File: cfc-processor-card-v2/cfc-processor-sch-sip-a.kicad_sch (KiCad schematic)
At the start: 33 parts, among them J5 Conn_01x04, Q1 MMBT2907, U10 TLVH431, U4 SN74AUC1G07DCKR, U7 OSD3358-1G-ISM

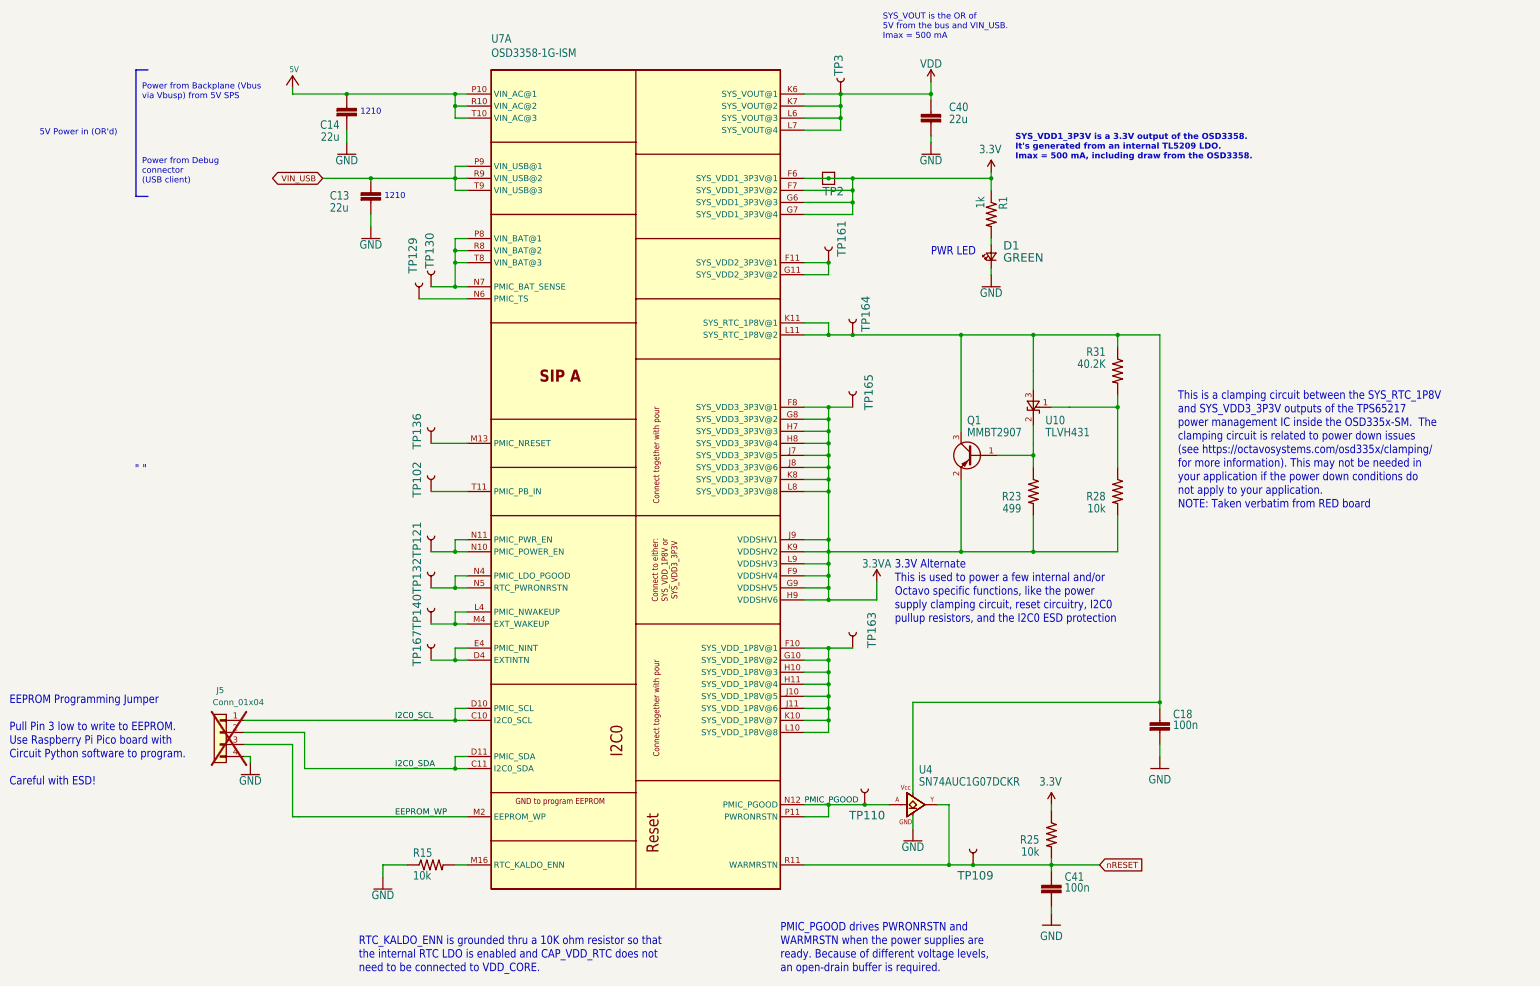
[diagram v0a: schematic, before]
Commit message: CFC processor schematic Change
changed to hierarchy view, changed all global net labels to hierarchy labels, changed all resistor, capacitor, and ground symbols to modern oresat labels. Deleted connectors sheet and added .history to gitignore.
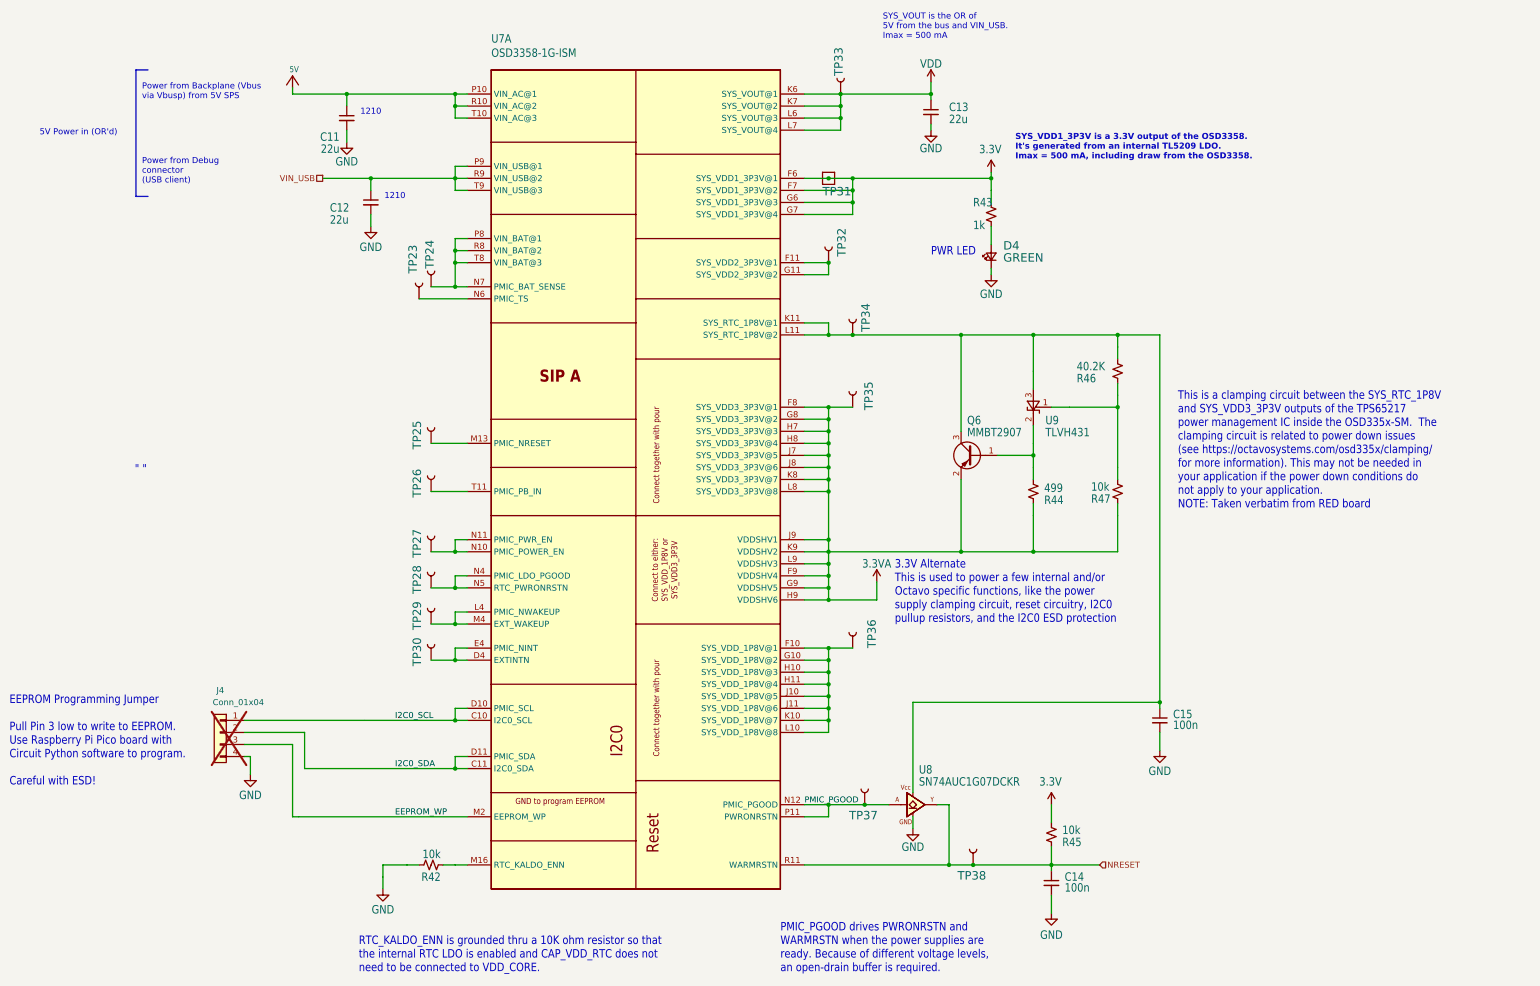
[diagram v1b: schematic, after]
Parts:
- C11: renamed from C14; symbol cfc-card-eagle-import:C-EUC1210 -> Device:C_Small
- C12: renamed from C13; symbol cfc-card-eagle-import:C-EUC1210 -> Device:C_Small
- C13: renamed from C40; symbol cfc-card-eagle-import:C-EUC1210 -> Device:C_Small
- C14: renamed from C41; symbol cfc-card-eagle-import:C-EU0603-A -> Device:C_Small
- C15: renamed from C18; symbol cfc-card-eagle-import:C-EU0603-A -> Device:C_Small
- R42: renamed from R15; symbol cfc-card-eagle-import:R-US_0603-A -> Device:R_Small_US
- R43: renamed from R1; symbol cfc-card-eagle-import:R-US_0603-A -> Device:R_Small_US
- R44: renamed from R23; symbol cfc-card-eagle-import:R-US_0603-A -> Device:R_Small_US
- R45: renamed from R25; symbol cfc-card-eagle-import:R-US_0603-A -> Device:R_Small_US
- R46: renamed from R31; symbol cfc-card-eagle-import:R-US_0603-A -> Device:R_Small_US
- R47: renamed from R28; symbol cfc-card-eagle-import:R-US_0603-A -> Device:R_Small_US
- renumbered D1 to D4, J5 to J4, Q1 to Q6, TP129 to TP23, TP130 to TP24, TP136 to TP25, TP102 to TP26, TP121 to TP27, TP132 to TP28, TP140 to TP29, TP167 to TP30, TP2 to TP31, TP161 to TP32, TP3 to TP33, TP164 to TP34, TP165 to TP35, TP163 to TP36, TP110 to TP37, TP109 to TP38, U4 to U8, U10 to U9
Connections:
- net nRESET renamed NRESET

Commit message: Updated OPD
couple of resistors and caps added to schematic. Changed USB ESD clamp VDD to 3.3v instead of octavo created VDD line.
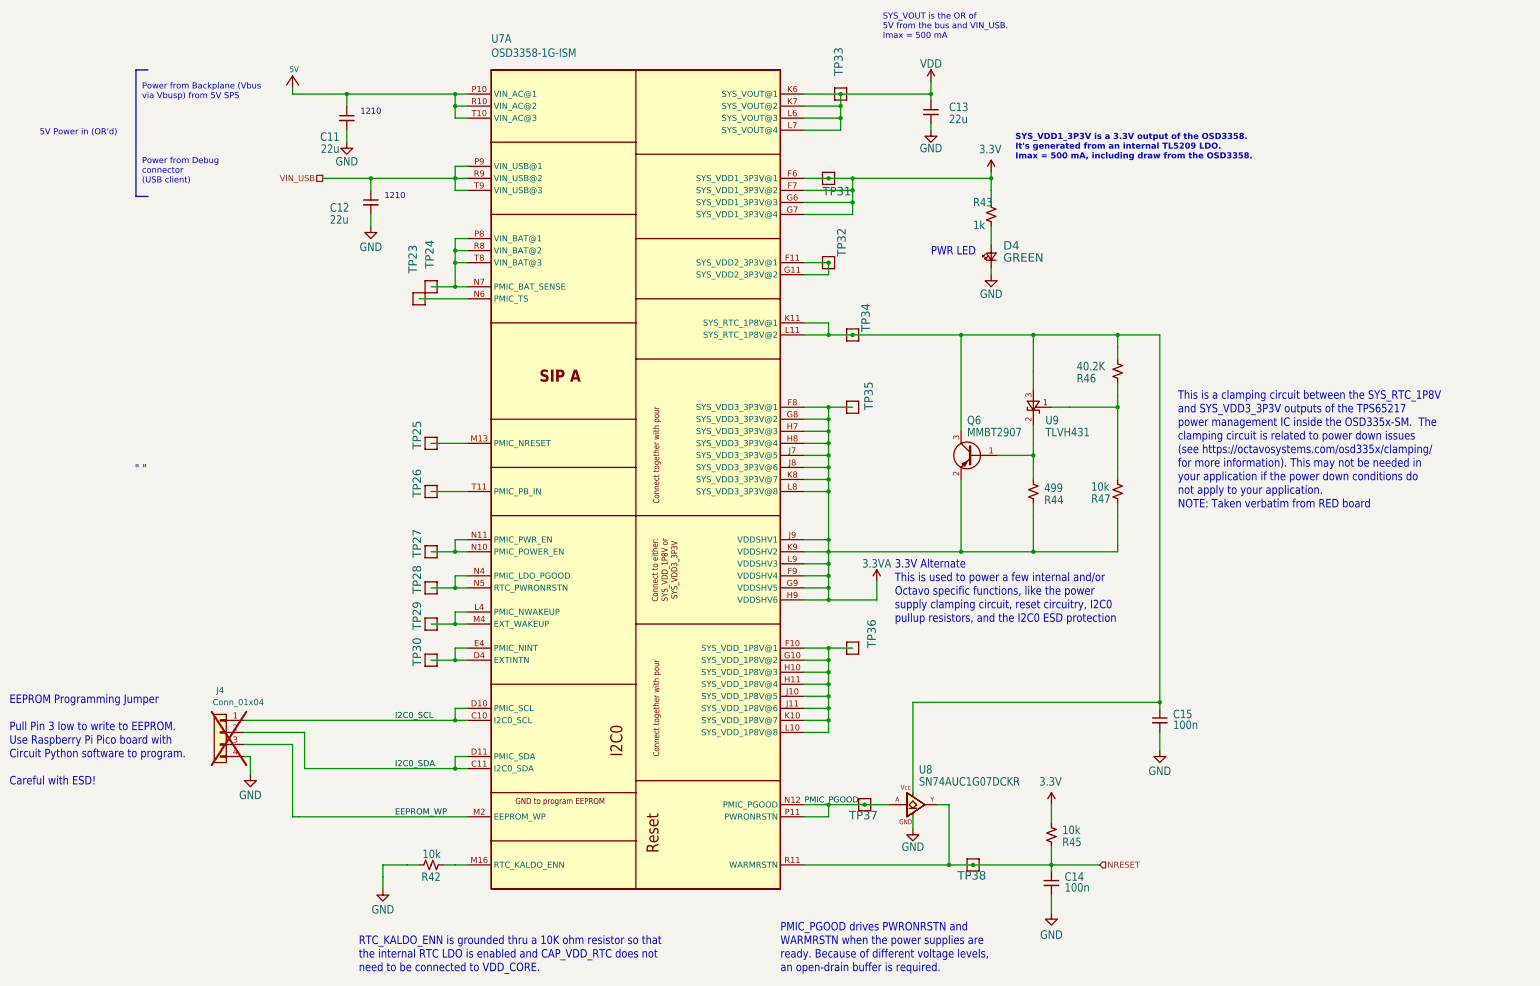
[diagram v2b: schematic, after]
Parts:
- TP23, TP24, TP25, TP26, TP27, TP28, TP29, TP30, TP32, TP33, TP34, TP35, TP36, TP37, TP38: footprint cfc-card:PAD.03X.04 -> oresat-misc:TestPoint_Pad_D1.0mm; symbol cfc-card-eagle-import:TEST-POINT3X4 -> Oresat Misc:Test-Point-1mm-round
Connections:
- net 3.3VA: now also TP35.1; no longer TP35.P$1 (1)
- net NRESET: now also TP38.1; no longer TP38.P$1 (1)
- net PMIC_PGOOD: now also TP37.1; no longer TP37.P$1 (1)
- net VDD: now also TP33.1; no longer TP33.P$1 (1)
- net at U7.D4 (EXTINTN), U7.E4 (PMIC_NINT): now also TP30.1; no longer TP30.P$1 (1)
- net at U7.F10 (SYS_VDD_1P8V@1), U7.G10 (SYS_VDD_1P8V@2), U7.H10 (SYS_VDD_1P8V@3)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: now also TP36.1; no longer TP36.P$1 (1)
- net at U7.F11 (SYS_VDD2_3P3V@1), U7.G11 (SYS_VDD2_3P3V@2): now also TP32.1; no longer TP32.P$1 (1)
- net at C15.1, Q6.3 (C), R46.1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: now also TP34.1; no longer TP34.P$1 (1)
- net at U7.L4 (PMIC_NWAKEUP), U7.M4 (EXT_WAKEUP): now also TP29.1; no longer TP29.P$1 (1)
- net at U7.M13 (PMIC_NRESET): now also TP25.1; no longer TP25.P$1 (1)
- net at U7.N10 (PMIC_POWER_EN), U7.N11 (PMIC_PWR_EN): now also TP27.1; no longer TP27.P$1 (1)
- net at U7.N4 (PMIC_LDO_PGOOD), U7.N5 (RTC_PWRONRSTN): now also TP28.1; no longer TP28.P$1 (1)
- net at U7.N6 (PMIC_TS): now also TP23.1; no longer TP23.P$1 (1)
- net at U7.N7 (PMIC_BAT_SENSE), U7.P8 (VIN_BAT@1), U7.R8 (VIN_BAT@2)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: now also TP24.1; no longer TP24.P$1 (1)
- net at U7.T11 (PMIC_PB_IN): now also TP26.1; no longer TP26.P$1 (1)

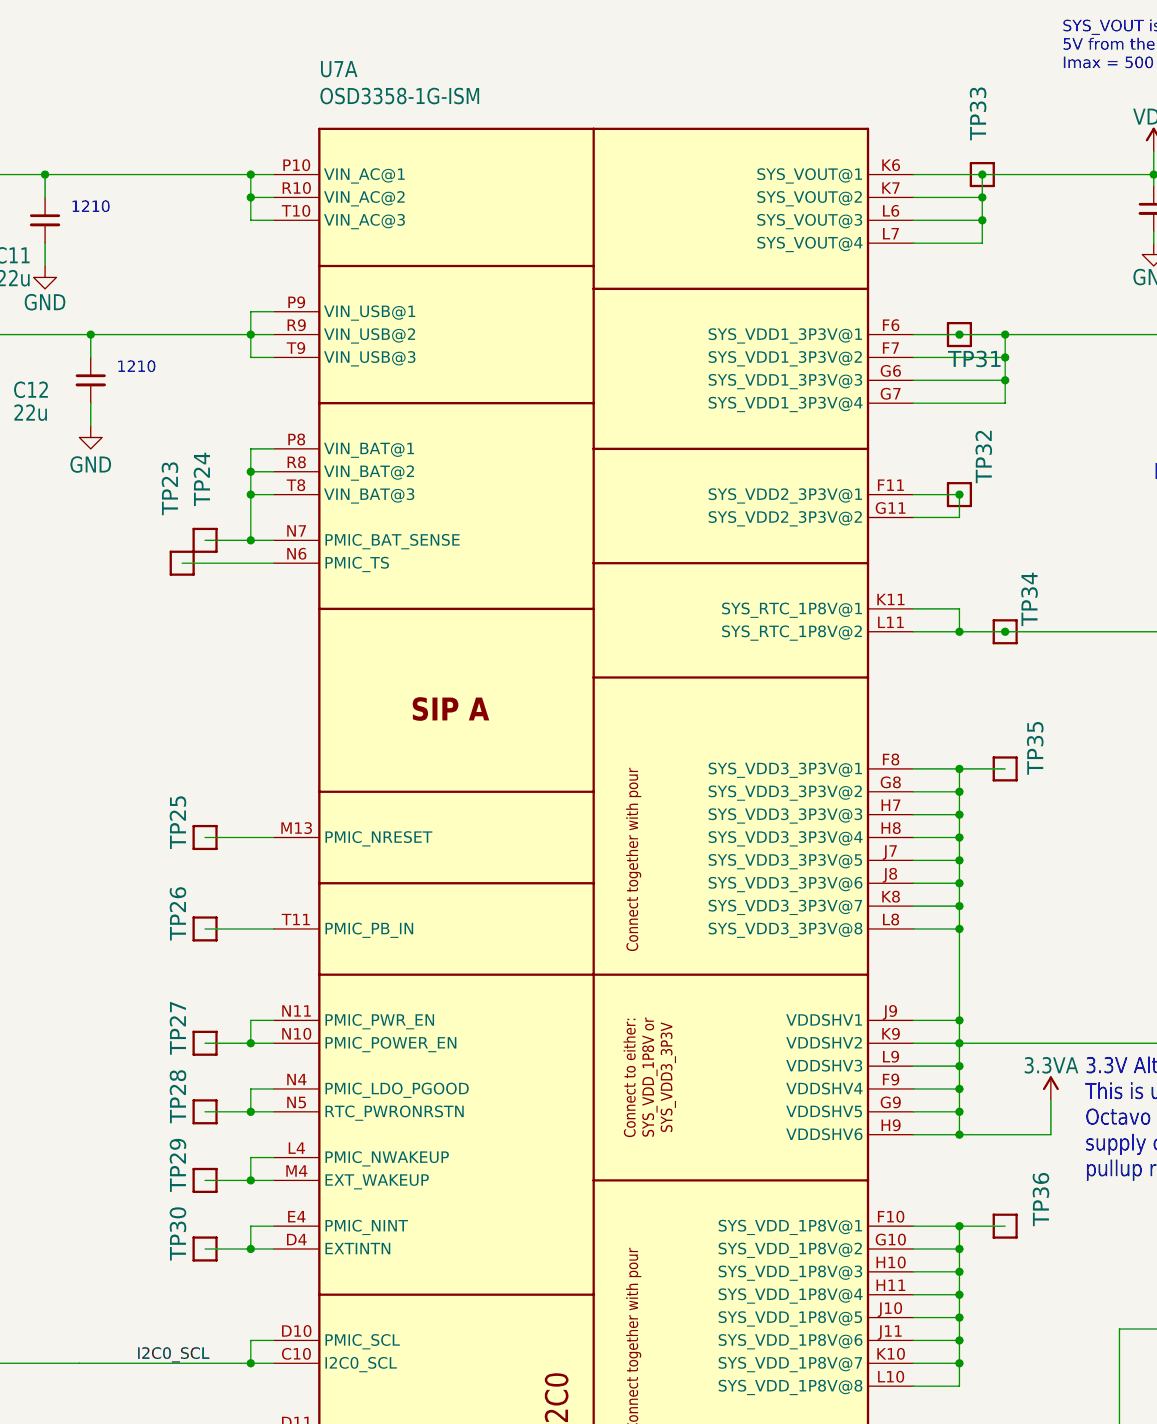
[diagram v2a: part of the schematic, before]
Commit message: Update
Added pull down resistors and removed therm + and sensor enable and added i2c support for cfc sensor card.
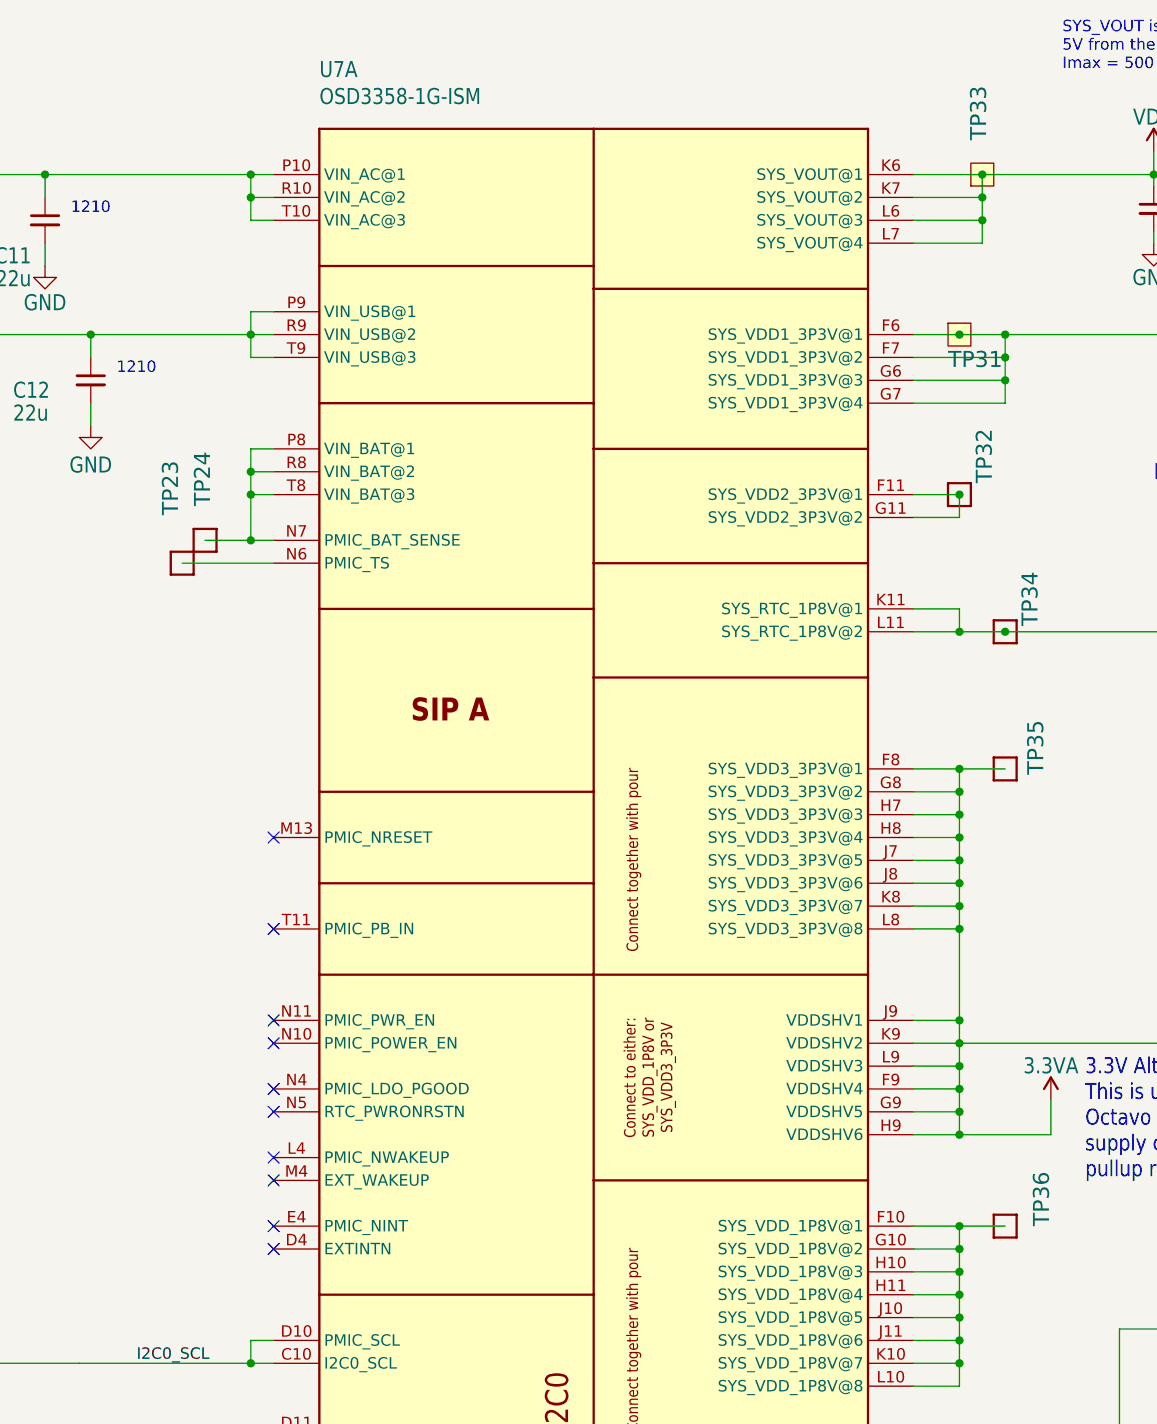
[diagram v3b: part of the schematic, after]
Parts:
- removed TP25, TP26, TP27, TP28, TP29, TP30: TEST-POINT3X4, oresat-misc:TestPoint_Pad_D1.0mm, symbol Oresat Misc:Test-Point-1mm-round
- TP31: footprint cfc-card:2MM-TEST-POINT -> oresat-misc:TestPoint-0.75mm-th; symbol cfc-card-eagle-import:TEST-POINT -> Oresat Misc:Test-Point-0.75mm-th
- TP33: footprint oresat-misc:TestPoint_Pad_D1.0mm -> oresat-misc:TestPoint-0.75mm-th; symbol Oresat Misc:Test-Point-1mm-round -> Oresat Misc:Test-Point-0.75mm-th
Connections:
- net at U7.D4 (EXTINTN): no longer U7.E4 (PMIC_NINT)
- net at U7.L4 (PMIC_NWAKEUP): no longer U7.M4 (EXT_WAKEUP)
- net at U7.N10 (PMIC_POWER_EN): no longer U7.N11 (PMIC_PWR_EN)
- net at U7.N4 (PMIC_LDO_PGOOD): no longer U7.N5 (RTC_PWRONRSTN)
- no-connect marks 0 -> 10
